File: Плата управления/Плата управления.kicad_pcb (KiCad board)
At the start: 6 copper layers, 67 x 72.7 mm, 123 parts, among them J1 A, J10 SWD, J2 B, J3 C, J4 Conn_01x10, J5 Conn_01x03_Pin, J6 Conn_01x02, J7 Conn_01x10, J8 Conn_01x02, J9 Conn_01x04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

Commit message: Добавил модель плты
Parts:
- added J11: C, Connector_My:Wire_one, F.Cu at (142.2, 107.7)
- added J12: C, Connector_My:Wire_one, F.Cu at (148.2, 107.7)
- added J13: C, Connector_My:Wire_one, F.Cu at (154.2, 107.7)
- added J14: C, Connector_My:Wire_one, F.Cu at (151.2, 107.7)
- added J15: C, Connector_My:Wire_one, F.Cu at (145.2, 107.7)
- J5: value Conn_01x03_Pin -> C; footprint Connector_PinHeader_2.54mm:PinHeader_1x03_P2.54mm_Vertical -> Connector_My:Wire_one
- moved J5 9.92 mm to (139.2, 107.7)
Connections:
- J5 pad 1: GND -> CAN1H
- U7 pad 29: PCB_Temp_C_MCU -> DAC_OUT1
- U7 pad 35: unconnected-(U7-PB0-Pad35) -> PCB_Temp_C_MCU
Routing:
- net CAN1H: track 35.7 -> 52.0 mm
- net CAN1L: track 35.2 -> 45.4 mm
- net +12V: track 81.4 -> 76.9 mm, vias 4 -> 5
- net DAC_OUT1: track 0.00 -> 3.86 mm, vias 0 -> 1
- net PCB_Temp_C_MCU: track 13.3 -> 11.3 mm
- removed copper zone on In2.Cu, net NTC_A+
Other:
- outline, holes or cut-outs redrawn

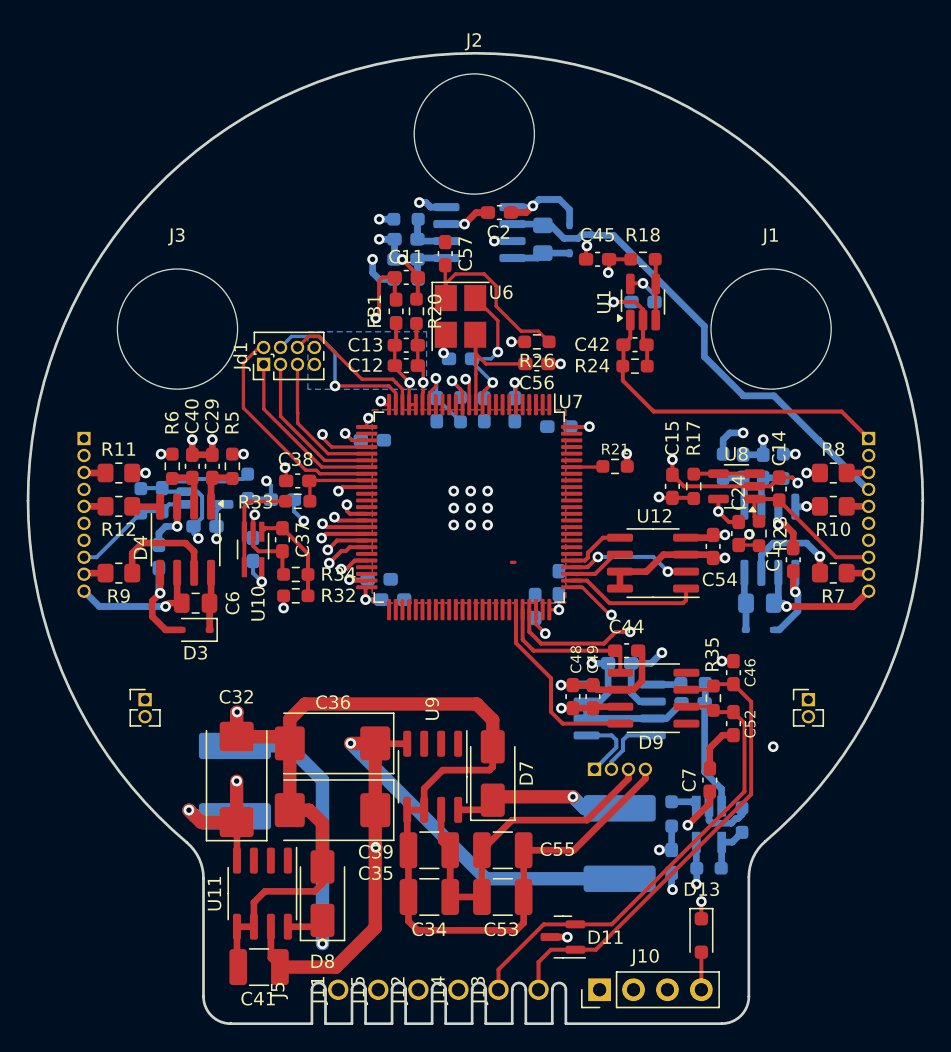
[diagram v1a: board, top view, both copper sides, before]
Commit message: Добавил все в BOM
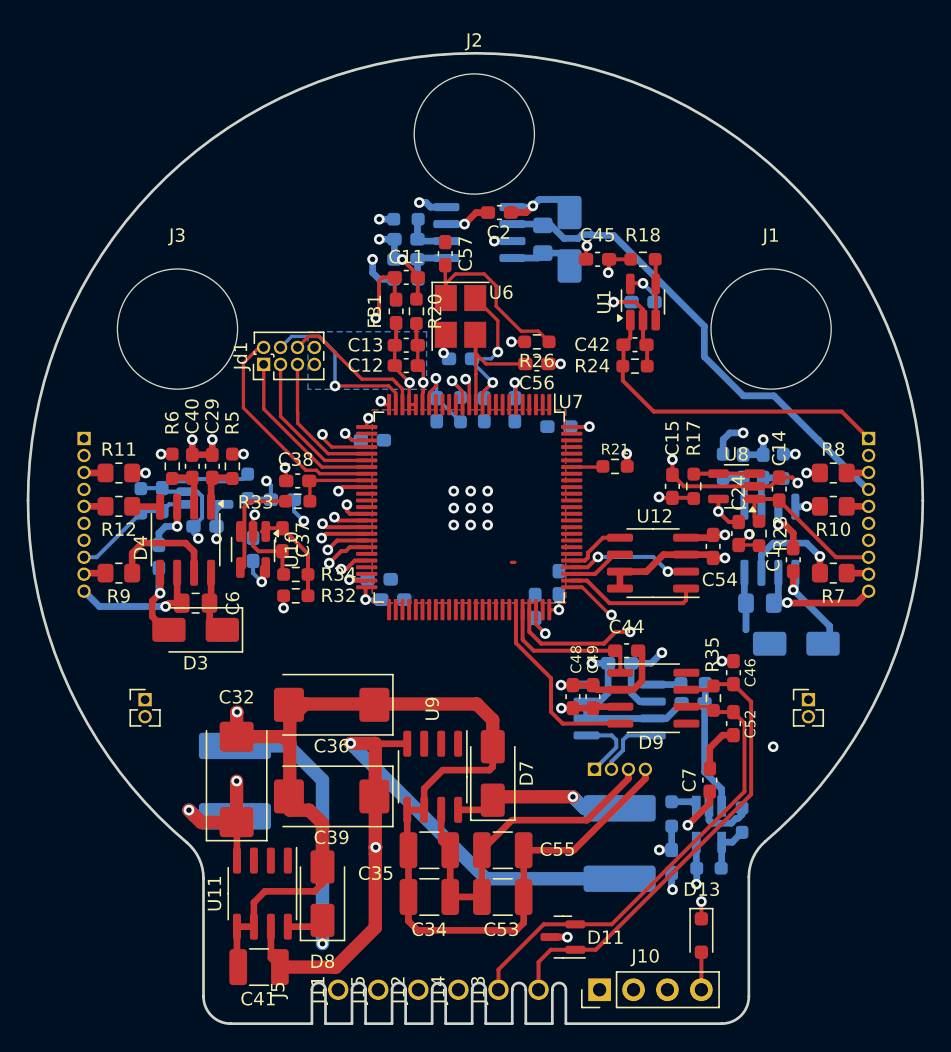
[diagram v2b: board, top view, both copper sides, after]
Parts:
- C16, C56, C57, C7, C8: value 0.1u -> 100n
- C36, C39: footprint Capacitor_Tantalum_SMD:CP_EIA-7343-31_Kemet-D_Pad2.25x2.55mm_HandSolder -> Capacitor_Tantalum_SMD:CP_EIA-7343-43_Kemet-X_Pad2.25x2.55mm_HandSolder
- D1, D2, D3: footprint Diode_SMD:D_SOD-323 -> Diode_SMD:D_SMA
- R13: value 1.3k -> 649
- U10: footprint Package_TO_SOT_SMD:SOT-353_SC-70-5_Handsoldering -> Package_TO_SOT_SMD:SOT-23-5_HandSoldering
- moved D1 2.92 mm to (173.5, 81.8)
- moved C36 2.89 mm to (138.7, 86.4)
- moved C39 1.03 mm to (138.7, 93.2)
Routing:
- net +12V: track 76.9 -> 77.8 mm

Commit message: Добавил съемные разъемы
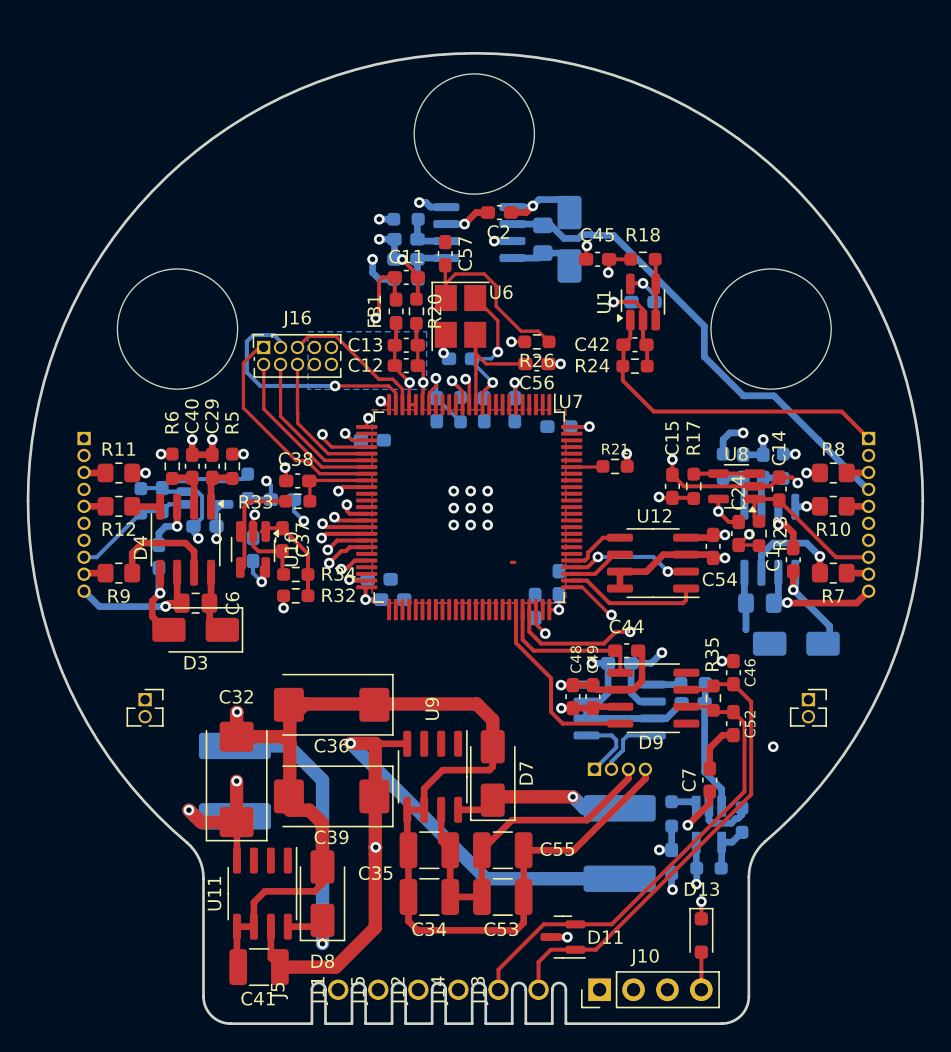
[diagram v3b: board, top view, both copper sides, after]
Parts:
- removed Jd1: Conn_02x04_Odd_Even, Connector_PinHeader_1.27mm:PinHeader_2x04_P1.27mm_Vertical
- added J16: Conn_02x05_Odd_Even, Connector_PinSocket_1.27mm:PinSocket_2x05_P1.27mm_Vertical, F.Cu at (133.6, 59.6)
- J6, J8: footprint Connector_PinHeader_1.27mm:PinHeader_1x02_P1.27mm_Vertical -> Connector_PinSocket_1.27mm:PinSocket_1x02_P1.27mm_Vertical
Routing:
- net NTC_A+: track 117.3 -> 132.7 mm
- net Temp_Coil_B_MCU: track 13.1 -> 18.3 mm
- added copper zone on In2.Cu, net GNDA

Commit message: Отправил на проверку в резонит
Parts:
- moved C57 7.75 mm to (151.3, 59.2), turned to 0 degrees
- moved R26 5.41 mm to (148.7, 60.1), turned to -90 degrees
- moved C16 4.77 mm to (150.4, 56.1), turned to 180 degrees
- moved C56 2.80 mm to (151.3, 61.0)
- moved C36 2.67 mm to (138.7, 89.0)
- moved C7 2.65 mm to (164.7, 93.3)
- moved U6 2.33 mm to (150.4, 56.1), turned to 0 degrees
- moved D2 1.80 mm to (157.4, 49.9)
- moved D3 0.91 mm to (128.5, 81.7)
- moved C39 0.89 mm to (138.7, 94.1)
- moved C37 0.38 mm to (135.4, 74.0)
- moved R32 0.27 mm to (136.3, 78.2)
- moved R34 0.27 mm to (136.3, 76.6)
- moved R14 0.13 mm to (169.5, 95.0)
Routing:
- net Net-(U6-Standby): track 14.6 -> 3.73 mm
- net +3.3V: track 83.4 -> 77.0 mm
- net Net-(U7-PH1): track 8.05 -> 3.01 mm, vias 2 -> 0
- net Net-(U6-Out): track 10.7 -> 14.0 mm
- net Net-(D1-K): track 4.33 -> 7.26 mm
- net DAC_OUT1: track 3.86 -> 5.64 mm
- net Net-(D3-K): track 4.33 -> 5.65 mm
- net CAN1H: track 52.0 -> 53.1 mm
- net +12V: track 77.8 -> 78.8 mm
- net CAN1L: track 45.4 -> 46.4 mm
- net GNDA: track 129.2 -> 128.6 mm, vias 8 -> 7
- net GND: track 170.4 -> 170.7 mm, vias 30 -> 34
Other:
- board text added: "G"
- board text added: "H"
- board text added: "L"

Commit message: Изменения: добавил папку с отчетностью
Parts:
- added R27: 0, Resistor_SMD:R_0603_1608Metric_Pad0.98x0.95mm_HandSolder, F.Cu at (148.1, 53.0)
- J16: footprint Connector_PinSocket_1.27mm:PinSocket_2x05_P1.27mm_Vertical -> Connector_PinHeader_1.27mm:PinHeader_2x05_P1.27mm_Vertical
- J6, J8: footprint Connector_PinSocket_1.27mm:PinSocket_1x02_P1.27mm_Vertical -> Connector_PinHeader_1.27mm:PinHeader_1x02_P1.27mm_Vertical
- moved J16 1.27 mm to (133.6, 60.9)
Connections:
- J16 pad 1: OUT_MCU -> Current_C_MCU
- J16 pad 10: NTC_A+ -> GNDA
- J16 pad 2: Current_C_MCU -> OUT_MCU
- J16 pad 3: Temp_Coil_B_MCU -> Current_B_MCU
- J16 pad 4: Current_B_MCU -> Temp_Coil_B_MCU
- J16 pad 5: Temp_Coil_A_MCU -> Current_A_MCU
- J16 pad 6: Current_A_MCU -> Temp_Coil_A_MCU
- J16 pad 7: GNDA -> NTC_A+
- J16 pad 8: NTC_A+ -> GNDA
- J16 pad 9: GNDA -> NTC_A+
- U6 pad 4: +3.3V -> Net-(U6-VDD)
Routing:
- net Net-(U6-VDD): track 0.00 -> 2.62 mm
- net +3.3V: track 77.0 -> 78.1 mm
